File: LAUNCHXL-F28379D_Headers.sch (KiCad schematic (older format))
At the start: 7 parts, among them U1 AMP_DUE_SCH

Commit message: LTSpice Simulation Finished
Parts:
- C2, C5: symbol Device:C -> PCB_2020-rescue:C-Device
- H1, H2, H3, H4: symbol Mechanical:MountingHole -> PCB_2020-rescue:MountingHole-Mechanical
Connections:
- net labels added: +12V-power, +3V3-power, +5V-power, GND-power
- net labels removed: +12V, +3V3, +5V, GND
- wire segments 23 -> 21
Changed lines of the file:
@@
 $EndDescr
 $Comp
-L Mechanical:MountingHole H1
+L PCB_2020-rescue:MountingHole-Mechanical H1
 U 1 1 5E1FD379
 P 1150 2200
@@
 $EndComp
 $Comp
-L Mechanical:MountingHole H2
+L PCB_2020-rescue:MountingHole-Mechanical H2
 U 1 1 5E27C5D4
 P 1150 2500
@@
 $EndComp
 $Comp
-L Mechanical:MountingHole H3
+L PCB_2020-rescue:MountingHole-Mechanical H3
 U 1 1 5E27C92D
 P 1150 2800
@@
 $EndComp
 $Comp
-L Mechanical:MountingHole H4
+L PCB_2020-rescue:MountingHole-Mechanical H4
 U 1 1 5E27CB44
 P 1150 3100
@@
 Decoupling Caps
 $Comp
-L power:+3V3 #+3V2
+L PCB_2020-rescue:+3V3-power #+3V2
 U 1 1 684850F5
 P 3300 5700
@@
 AR Path="/5DF27589/684850F5" Ref="#+3V02"  Part="1"
 F 0 "#+3V02" H 3300 5700 50  0001 C CNN
-F 1 "+3V3" H 3150 5850 59  0000 L BNN
+F 1 "+3V3-power" H 3150 5850 59  0000 L BNN
 F 2 "" H 3300 5700 50  0001 C CNN
 F 3 "" H 3300 5700 50  0001 C CNN
@@
 $EndComp
 $Comp
-L Device:C C2
+L PCB_2020-rescue:C-Device C2
 U 1 1 6A2D04C9
 P 3300 6100
@@
 $EndComp
 $Comp
-L power:GND #GND3
+L PCB_2020-rescue:GND-power #GND3
 U 1 1 E2B99DEF
 P 4050 6500
@@
 AR Path="/5DF27589/E2B99DEF" Ref="#GND03"  Part="1"
 F 0 "#GND03" H 4050 6500 50  0001 C CNN
-F 1 "GND" H 3950 6300 59  0000 L BNN
+F 1 "GND-power" H 3950 6300 59  0000 L BNN
 F 2 "" H 4050 6500 50  0001 C CNN
 F 3 "" H 4050 6500 50  0001 C CNN
@@
 	1    0    0    -1
 $EndComp
-Wire Wire Line
-	3300 6500 4050 6500
-$Comp
-L Device:C C5
+$Comp
+L PCB_2020-rescue:C-Device C5
 U 1 1 6C4A4E38
 P 4750 6100
@@
 	4750 6250 4750 6500
 $Comp
-L power:+12V #PWR0101
+L PCB_2020-rescue:+12V-power #PWR0101
 U 1 1 5E5B7DE1
 P 4750 5700
 F 0 "#PWR0101" H 4750 5550 50  0001 C CNN
-F 1 "+12V" H 4650 5900 50  0000 L CNN
+F 1 "+12V-power" H 4650 5900 50  0000 L CNN
 F 2 "" H 4750 5700 50  0001 C CNN
 F 3 "" H 4750 5700 50  0001 C CNN
@@
 	3300 6250 3300 6500
 Connection ~ 4050 6500
-Wire Wire Line
-	4050 6500 4100 6500
-Wire Wire Line
-	4050 6500 4750 6500
 $Comp
 L PCB_2020:AMP_DUE_SCH U1
@@
 	8650 3400 8750 3400
 Wire Wire Line
-	7700 2750 7800 2750
-Connection ~ 7700 2750
-Wire Wire Line
 	7800 2750 7800 2850
-Wire Wire Line
-	7650 2750 7700 2750
 Wire Wire Line
 	7650 2850 7650 2750
@@
 KS1_CTL
 $Comp
-L power:+12V #PWR01
+L PCB_2020-rescue:+12V-power #PWR01
 U 1 1 5E686230
 P 7950 2850
 F 0 "#PWR01" H 7950 2700 50  0001 C CNN
-F 1 "+12V" H 7850 3050 50  0000 L CNN
+F 1 "+12V-power" H 7850 3050 50  0000 L CNN
 F 2 "" H 7950 2850 50  0001 C CNN
 F 3 "" H 7950 2850 50  0001 C CNN
@@
 $EndComp
 $Comp
-L power:+5V #P+?
+L PCB_2020-rescue:+5V-power #P+?
 U 1 1 5E684B6F
 P 7500 2850
@@
 AR Path="/5DF27589/5E684B6F" Ref="#P+06"  Part="1"
 F 0 "#P+06" H 7500 2850 50  0001 C CNN
-F 1 "+5V" H 7400 3000 59  0000 L BNN
+F 1 "+5V-power" H 7400 3000 59  0000 L BNN
 F 2 "" H 7500 2850 50  0001 C CNN
 F 3 "" H 7500 2850 50  0001 C CNN
@@
 $EndComp
 $Comp
-L power:GND #GND?
+L PCB_2020-rescue:GND-power #GND?
 U 1 1 5E681F81
 P 7700 2750
@@
 AR Path="/5DF27589/5E681F81" Ref="#GND04"  Part="1"
 F 0 "#GND04" H 7700 2750 50  0001 C CNN
-F 1 "GND" H 7600 2550 59  0000 L BNN
+F 1 "GND-power" H 7600 2550 59  0000 L BNN
 F 2 "" H 7700 2750 50  0001 C CNN
 F 3 "" H 7700 2750 50  0001 C CNN
@@
 Text GLabel 8750 3500 2    39   BiDi ~ 0
 SCIB_RX
+Wire Wire Line
+	3300 6500 4050 6500
+Wire Wire Line
+	7650 2750 7800 2750
+Wire Wire Line
+	4050 6500 4750 6500
 $EndSCHEMATC

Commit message: Updating PCB
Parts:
- removed U1: AMP_DUE_SCH, Drivetrain_control:Arduino DUE, symbol PCB_2020:AMP_DUE_SCH
- added U1: AMP_DUE_SCH, Drivetrain_control:Arduino DUE, symbol PCB_2020:AMP_DUE_SCH
- C2, C5: footprint Capacitor_SMD:C_0805_2012Metric_Pad1.15x1.40mm_HandSolder -> Capacitor_SMD:C_0805_2012Metric_Pad1.18x1.45mm_HandSolder
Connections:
- net +12V: now also U1.7 (GND)
- net +5V: now also U1.4 (3V3)
- net Brake_PWM_1: now also U1.78 (D9)
- net Brake_PWM_2: now also U1.77 (D8)
- net EN+_CTL: now also U1.47 (D29)
- net FS1_CTL: now also U1.53 (D41)
- net FWD_CTL: now also U1.56 (D47)
- net GND: now also U1.5 (5V), U1.6 (GND)
- net INPUT_A+_CTL: now also U1.50 (D35)
- net KS1_CTL: now also U1.59 (D53)
- net REV_CTL: now also U1.44 (D23)
- net SCIB_RX: now also U1.69 (RX0_0)
- net SCIB_TX: now also U1.70 (TX0_1)
- net STEERING: now also U1.76 (D7)
- net THROTTLE: now also U1.20 (A11)
- no-connect marks 2 -> 69
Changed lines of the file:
@@
 F 0 "C2" H 3360 6115 59  0000 L BNN
 F 1 "0.1uF" H 3360 5915 59  0000 L BNN
-F 2 "Capacitor_SMD:C_0805_2012Metric_Pad1.15x1.40mm_HandSolder" H 3300 6100 50  0001 C CNN
+F 2 "Capacitor_SMD:C_0805_2012Metric_Pad1.18x1.45mm_HandSolder" H 3300 6100 50  0001 C CNN
 F 3 "https://www.digikey.com/product-detail/en/samsung-electro-mechanics/CL21B104JBCNNNC/1276-1090-1-ND/3889176?utm_adgroup=Capacitors&slid=&pdv=c&pcrid=398891859082&productid=&utm_campaign=Dynamic+Search&mkwid=sK4nOncLn&utm_medium=cpc&utm_term=&gclid=CjwKCAiAmNbwBRBOEiwAqcwwpZSQgtNujl6BHsUYP-FQ70zdNcKZbQcVdbZiRuST7tQ2_ezynANN3xoCFdYQAvD_BwE&pmt=b&pkw=&utm_source=google" H 3300 6100 50  0001 C CNN
 	1    3300 6100
@@
 F 0 "C5" H 4810 6115 59  0000 L BNN
 F 1 "0.1uF" H 4810 5915 59  0000 L BNN
-F 2 "Capacitor_SMD:C_0805_2012Metric_Pad1.15x1.40mm_HandSolder" H 4750 6100 50  0001 C CNN
+F 2 "Capacitor_SMD:C_0805_2012Metric_Pad1.18x1.45mm_HandSolder" H 4750 6100 50  0001 C CNN
 F 3 "https://www.digikey.com/product-detail/en/samsung-electro-mechanics/CL21B104JBCNNNC/1276-1090-1-ND/3889176?utm_adgroup=Capacitors&slid=&pdv=c&pcrid=398891859082&productid=&utm_campaign=Dynamic+Search&mkwid=sK4nOncLn&utm_medium=cpc&utm_term=&gclid=CjwKCAiAmNbwBRBOEiwAqcwwpZSQgtNujl6BHsUYP-FQ70zdNcKZbQcVdbZiRuST7tQ2_ezynANN3xoCFdYQAvD_BwE&pmt=b&pkw=&utm_source=google" H 4750 6100 50  0001 C CNN
 	1    4750 6100
@@
 	3300 6250 3300 6500
 Connection ~ 4050 6500
-$Comp
-L PCB_2020:AMP_DUE_SCH U1
-U 6 1 5E7098FE
-P 7650 3400
-F 0 "U1" H 6606 3446 50  0000 R CNN
-F 1 "AMP_DUE_SCH" H 6606 3355 50  0000 R CNN
-F 2 "Drivetrain_control:Arduino DUE" H 7650 3400 50  0001 C CNN
-F 3 "" H 8200 3300 50  0001 C CNN
-	6    7650 3400
-	1    0    0    -1
-$EndComp
-NoConn ~ 7350 2850
-Wire Wire Line
-	8650 3500 8750 3500
-Wire Wire Line
-	8650 3400 8750 3400
-Wire Wire Line
-	7800 2750 7800 2850
-Wire Wire Line
-	7650 2850 7650 2750
-NoConn ~ 6650 3400
-Text GLabel 6950 4100 3    39   BiDi ~ 0
+Wire Wire Line
+	10500 3300 10600 3300
+Wire Wire Line
+	10500 3200 10600 3200
+Text GLabel 7000 4600 3    39   BiDi ~ 0
 KS1_CTL
 $Comp
 L PCB_2020-rescue:+12V-power #PWR01
 U 1 1 5E686230
-P 7950 2850
-F 0 "#PWR01" H 7950 2700 50  0001 C CNN
-F 1 "+12V-power" H 7850 3050 50  0000 L CNN
-F 2 "" H 7950 2850 50  0001 C CNN
-F 3 "" H 7950 2850 50  0001 C CNN
-	1    7950 2850
-	1    0    0    -1
+P 6050 2200
+F 0 "#PWR01" H 6050 2050 50  0001 C CNN
+F 1 "+12V-power" H 5950 2400 50  0000 L CNN
+F 2 "" H 6050 2200 50  0001 C CNN
+F 3 "" H 6050 2200 50  0001 C CNN
+	1    6050 2200
+	0    -1   -1   0
 $EndComp
 $Comp
 L PCB_2020-rescue:+5V-power #P+?
 U 1 1 5E684B6F
-P 7500 2850
+P 6350 1900
 AR Path="/5E684B6F" Ref="#P+?"  Part="1"
 AR Path="/5DF27589/5E684B6F" Ref="#P+06"  Part="1"
-F 0 "#P+06" H 7500 2850 50  0001 C CNN
-F 1 "+5V-power" H 7400 3000 59  0000 L BNN
-F 2 "" H 7500 2850 50  0001 C CNN
-F 3 "" H 7500 2850 50  0001 C CNN
-	1    7500 2850
-	1    0    0    -1
+F 0 "#P+06" H 6350 1900 50  0001 C CNN
+F 1 "+5V-power" H 6250 2050 59  0000 L BNN
+F 2 "" H 6350 1900 50  0001 C CNN
+F 3 "" H 6350 1900 50  0001 C CNN
+	1    6350 1900
+	0    -1   -1   0
 $EndComp
 $Comp
 L PCB_2020-rescue:GND-power #GND?
 U 1 1 5E681F81
-P 7700 2750
+P 6350 2100
 AR Path="/5E681F81" Ref="#GND?"  Part="1"
 AR Path="/5DF27589/5E681F81" Ref="#GND04"  Part="1"
-F 0 "#GND04" H 7700 2750 50  0001 C CNN
-F 1 "GND-power" H 7600 2550 59  0000 L BNN
-F 2 "" H 7700 2750 50  0001 C CNN
-F 3 "" H 7700 2750 50  0001 C CNN
-	1    7700 2750
-	-1   0    0    1
-$EndComp
-Wire Wire Line
-	8650 3300 8750 3300
-Wire Wire Line
-	8650 3200 8750 3200
-Wire Wire Line
-	8650 3100 8750 3100
-Wire Wire Line
-	6450 3300 6650 3300
-Text GLabel 6450 3300 0    39   Output ~ 0
+F 0 "#GND04" H 6350 2100 50  0001 C CNN
+F 1 "GND-power" H 6250 1900 59  0000 L BNN
+F 2 "" H 6350 2100 50  0001 C CNN
+F 3 "" H 6350 2100 50  0001 C CNN
+	1    6350 2100
+	0    1    1    0
+$EndComp
+Wire Wire Line
+	10500 2600 10600 2600
+Wire Wire Line
+	10500 2500 10600 2500
+Wire Wire Line
+	10500 2400 10600 2400
+Text GLabel 6450 3500 0    39   Output ~ 0
 THROTTLE
-Wire Wire Line
-	7250 3950 7250 4100
-Wire Wire Line
-	7550 3950 7550 4100
-Wire Wire Line
-	7850 3950 7850 4100
-Text GLabel 8450 4100 3    39   BiDi ~ 0
+Text GLabel 10000 4600 3    39   BiDi ~ 0
 REV_CTL
-Text GLabel 7250 4100 3    39   BiDi ~ 0
+Text GLabel 7600 4600 3    39   BiDi ~ 0
 FWD_CTL
-Text GLabel 7550 4100 3    39   BiDi ~ 0
+Text GLabel 8200 4600 3    39   BiDi ~ 0
 FS1_CTL
-Text GLabel 7850 4100 3    39   Input ~ 0
+Text GLabel 8800 4600 3    39   Input ~ 0
 INPUT_A+_CTL
-Text GLabel 8150 4100 3    39   Output ~ 0
+Text GLabel 9400 4600 3    39   Output ~ 0
 EN+_CTL
-Text GLabel 8750 3300 2    39   BiDi ~ 0
+Text GLabel 10600 2600 2    39   BiDi ~ 0
 STEERING
-Wire Wire Line
-	8450 4100 8450 3950
-Wire Wire Line
-	6950 4100 6950 3950
-Wire Wire Line
-	8150 4100 8150 3950
-Text GLabel 8750 3200 2    39   Output ~ 0
+Text GLabel 10600 2500 2    39   Output ~ 0
 Brake_PWM_2
-Text GLabel 8750 3100 2    39   Output ~ 0
+Text GLabel 10600 2400 2    39   Output ~ 0
 Brake_PWM_1
-Text GLabel 8750 3400 2    39   BiDi ~ 0
+Text GLabel 10600 3200 2    39   BiDi ~ 0
 SCIB_TX
-Text GLabel 8750 3500 2    39   BiDi ~ 0
+Text GLabel 10600 3300 2    39   BiDi ~ 0
 SCIB_RX
 Wire Wire Line
 	3300 6500 4050 6500
 Wire Wire Line
-	7650 2750 7800 2750
-Wire Wire Line
 	4050 6500 4750 6500
+$Comp
+L PCB_2020:AMP_DUE_SCH U1
+U 1 1 5F87F561
+P 8550 3050
+F 0 "U1" H 8550 4915 50  0000 C CNN
+F 1 "AMP_DUE_SCH" H 8550 4824 50  0000 C CNN
+F 2 "Drivetrain_control:Arduino DUE" H 8550 3050 50  0001 C CNN
+F 3 "" H 9100 2950 50  0001 C CNN
+	1    8550 3050
+	1    0    0    -1
+$EndComp
+Wire Wire Line
+	6450 3500 6600 3500
+Wire Wire Line
+	7000 4600 7000 4450
+Wire Wire Line
+	7600 4600 7600 4450
+Wire Wire Line
+	8200 4600 8200 4450
+Wire Wire Line
+	8800 4450 8800 4600
+Wire Wire Line
+	9400 4450 9400 4600
+Wire Wire Line
+	10000 4600 10000 4450
+Wire Wire Line
+	6350 1900 6600 1900
+Wire Wire Line
+	6350 2100 6500 2100
+Wire Wire Line
+	6500 2100 6500 2000
+Wire Wire Line
+	6500 2000 6600 2000
+Connection ~ 6500 2100
+Wire Wire Line
+	6500 2100 6600 2100
+Wire Wire Line
+	6050 2200 6600 2200
+NoConn ~ 6600 1600
+NoConn ~ 6600 1700
+NoConn ~ 6600 1800
+NoConn ~ 6600 2300
+NoConn ~ 6600 2400
+NoConn ~ 6600 2500
+NoConn ~ 6600 2600
+NoConn ~ 6600 2700
+NoConn ~ 6600 2800
+NoConn ~ 6600 2900
+NoConn ~ 6600 3000
+NoConn ~ 6600 3100
+NoConn ~ 6600 3200
+NoConn ~ 6600 3300
+NoConn ~ 6600 3400
+NoConn ~ 6600 3600
+NoConn ~ 6600 3700
+NoConn ~ 6600 3800
+NoConn ~ 6800 4450
+NoConn ~ 6900 4450
+NoConn ~ 7100 4450
+NoConn ~ 7200 4450
+NoConn ~ 7300 4450
+NoConn ~ 7400 4450
+NoConn ~ 7500 4450
+NoConn ~ 7700 4450
+NoConn ~ 7800 4450
+NoConn ~ 7900 4450
+NoConn ~ 8000 4450
+NoConn ~ 8100 4450
+NoConn ~ 8300 4450
+NoConn ~ 8400 4450
+NoConn ~ 8500 4450
+NoConn ~ 8600 4450
+NoConn ~ 8700 4450
+NoConn ~ 8900 4450
+NoConn ~ 9000 4450
+NoConn ~ 9100 4450
+NoConn ~ 9200 4450
+NoConn ~ 10500 1600
+NoConn ~ 10500 1700
+NoConn ~ 10500 1800
+NoConn ~ 10500 1900
+NoConn ~ 10500 2000
+NoConn ~ 10500 2100
+NoConn ~ 10500 2200
+NoConn ~ 10500 2300
+NoConn ~ 10500 2700
+NoConn ~ 10500 2800
+NoConn ~ 10500 2900
+NoConn ~ 10500 3000
+NoConn ~ 10500 3100
+NoConn ~ 10500 3400
+NoConn ~ 10500 3500
+NoConn ~ 10500 3600
+NoConn ~ 10500 3700
+NoConn ~ 10500 3800
+NoConn ~ 10500 3900
+NoConn ~ 10500 4000
+NoConn ~ 10500 4100
+NoConn ~ 9300 4450
+NoConn ~ 9500 4450
+NoConn ~ 9600 4450
+NoConn ~ 9700 4450
+NoConn ~ 9800 4450
+NoConn ~ 9900 4450
+NoConn ~ 10100 4450
+NoConn ~ 10200 4450
+NoConn ~ 10300 4450
 $EndSCHEMATC

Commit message: Working on PCB Routing for LoRa
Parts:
- added U4: LoRa, Drivetrain_control:LoRa, symbol PCB_2020-rescue:LoRa
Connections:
- net +3V3: now also U1.3 (IOREF), U4.48 (3V3)
- net GND: now also U4.49 (GND)
- no-connect marks 69 -> 68
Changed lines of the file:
@@
 NoConn ~ 6600 1600
 NoConn ~ 6600 1700
-NoConn ~ 6600 1800
 NoConn ~ 6600 2300
 NoConn ~ 6600 2400
@@
 NoConn ~ 10200 4450
 NoConn ~ 10300 4450
+$Comp
+L PCB_2020-rescue:LoRa U4
+U 1 1 5FA8EB82
+P 4050 3550
+F 0 "U4" H 4050 4615 50  0000 C CNN
+F 1 "LoRa" H 4050 4524 50  0000 C CNN
+F 2 "Drivetrain_control:LoRa" H 4050 3950 50  0001 C CNN
+F 3 "" H 4050 3950 50  0001 C CNN
+	1    4050 3550
+	1    0    0    -1
+$EndComp
+$Comp
+L PCB_2020-rescue:+3V3-power #PWR?
+U 1 1 5FAB7823
+P 6400 1800
+F 0 "#PWR?" H 6400 1650 50  0001 C CNN
+F 1 "+3V3-power" H 6415 1973 50  0000 C CNN
+F 2 "" H 6400 1800 50  0001 C CNN
+F 3 "" H 6400 1800 50  0001 C CNN
+	1    6400 1800
+	1    0    0    -1
+$EndComp
+Wire Wire Line
+	6400 1800 6600 1800
+Connection ~ 6300 2100
+$Comp
+L PCB_2020-rescue:GND-power #PWR?
+U 1 1 5FABAD06
+P 3500 3100
+F 0 "#PWR?" H 3500 2850 50  0001 C CNN
+F 1 "GND-power" V 3505 2973 50  0000 R CNN
+F 2 "" H 3500 3100 50  0001 C CNN
+F 3 "" H 3500 3100 50  0001 C CNN
+	1    3500 3100
+	0    1    1    0
+$EndComp
+$Comp
+L PCB_2020-rescue:+3V3-power #PWR?
+U 1 1 5FABBDB9
+P 3500 2900
+F 0 "#PWR?" H 3500 2750 50  0001 C CNN
+F 1 "+3V3-power" V 3515 3027 50  0000 L CNN
+F 2 "" H 3500 2900 50  0001 C CNN
+F 3 "" H 3500 2900 50  0001 C CNN
+	1    3500 2900
+	0    -1   -1   0
+$EndComp
 $EndSCHEMATC

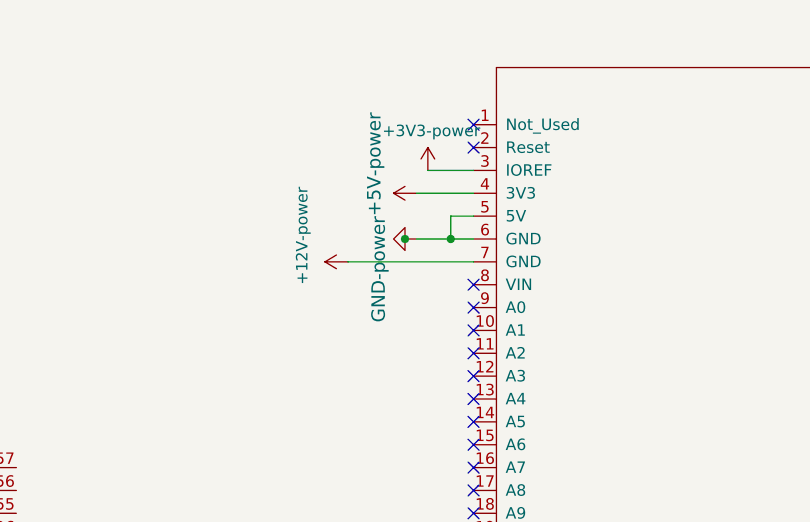
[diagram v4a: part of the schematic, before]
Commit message: Updating PCB with LoRa
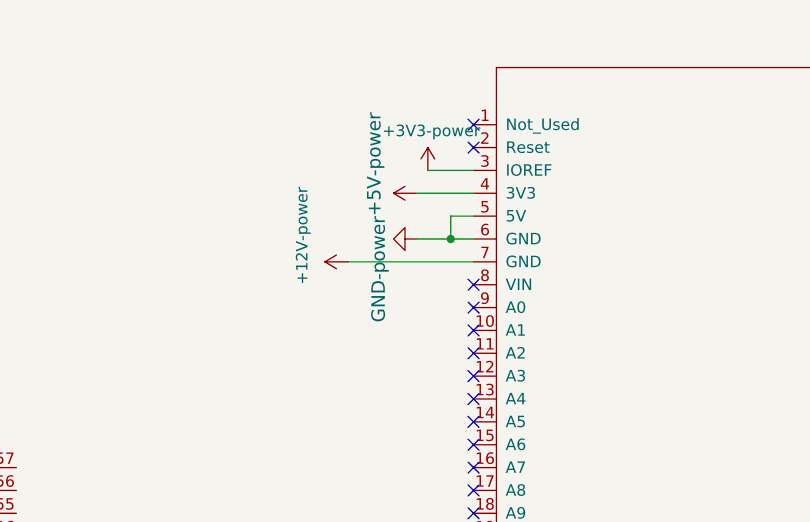
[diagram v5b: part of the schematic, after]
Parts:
- C2, C5: footprint Capacitor_SMD:C_0805_2012Metric_Pad1.18x1.45mm_HandSolder -> Capacitor_THT:C_Disc_D3.0mm_W1.6mm_P2.50mm
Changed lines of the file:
@@
 F 0 "C2" H 3360 6115 59  0000 L BNN
 F 1 "0.1uF" H 3360 5915 59  0000 L BNN
-F 2 "Capacitor_SMD:C_0805_2012Metric_Pad1.18x1.45mm_HandSolder" H 3300 6100 50  0001 C CNN
+F 2 "Capacitor_THT:C_Disc_D3.0mm_W1.6mm_P2.50mm" H 3300 6100 50  0001 C CNN
 F 3 "https://www.digikey.com/product-detail/en/samsung-electro-mechanics/CL21B104JBCNNNC/1276-1090-1-ND/3889176?utm_adgroup=Capacitors&slid=&pdv=c&pcrid=398891859082&productid=&utm_campaign=Dynamic+Search&mkwid=sK4nOncLn&utm_medium=cpc&utm_term=&gclid=CjwKCAiAmNbwBRBOEiwAqcwwpZSQgtNujl6BHsUYP-FQ70zdNcKZbQcVdbZiRuST7tQ2_ezynANN3xoCFdYQAvD_BwE&pmt=b&pkw=&utm_source=google" H 3300 6100 50  0001 C CNN
 	1    3300 6100
@@
 F 0 "C5" H 4810 6115 59  0000 L BNN
 F 1 "0.1uF" H 4810 5915 59  0000 L BNN
-F 2 "Capacitor_SMD:C_0805_2012Metric_Pad1.18x1.45mm_HandSolder" H 4750 6100 50  0001 C CNN
+F 2 "Capacitor_THT:C_Disc_D3.0mm_W1.6mm_P2.50mm" H 4750 6100 50  0001 C CNN
 F 3 "https://www.digikey.com/product-detail/en/samsung-electro-mechanics/CL21B104JBCNNNC/1276-1090-1-ND/3889176?utm_adgroup=Capacitors&slid=&pdv=c&pcrid=398891859082&productid=&utm_campaign=Dynamic+Search&mkwid=sK4nOncLn&utm_medium=cpc&utm_term=&gclid=CjwKCAiAmNbwBRBOEiwAqcwwpZSQgtNujl6BHsUYP-FQ70zdNcKZbQcVdbZiRuST7tQ2_ezynANN3xoCFdYQAvD_BwE&pmt=b&pkw=&utm_source=google" H 4750 6100 50  0001 C CNN
 	1    4750 6100
@@
 $EndComp
 $Comp
-L PCB_2020-rescue:+3V3-power #PWR?
+L PCB_2020-rescue:+3V3-power #PWR0108
 U 1 1 5FAB7823
 P 6400 1800
-F 0 "#PWR?" H 6400 1650 50  0001 C CNN
+F 0 "#PWR0108" H 6400 1650 50  0001 C CNN
 F 1 "+3V3-power" H 6415 1973 50  0000 C CNN
 F 2 "" H 6400 1800 50  0001 C CNN
@@
 Wire Wire Line
 	6400 1800 6600 1800
-Connection ~ 6300 2100
-$Comp
-L PCB_2020-rescue:GND-power #PWR?
+$Comp
+L PCB_2020-rescue:GND-power #PWR0109
 U 1 1 5FABAD06
 P 3500 3100
-F 0 "#PWR?" H 3500 2850 50  0001 C CNN
+F 0 "#PWR0109" H 3500 2850 50  0001 C CNN
 F 1 "GND-power" V 3505 2973 50  0000 R CNN
 F 2 "" H 3500 3100 50  0001 C CNN
@@
 $EndComp
 $Comp
-L PCB_2020-rescue:+3V3-power #PWR?
+L PCB_2020-rescue:+3V3-power #PWR0110
 U 1 1 5FABBDB9
 P 3500 2900
-F 0 "#PWR?" H 3500 2750 50  0001 C CNN
+F 0 "#PWR0110" H 3500 2750 50  0001 C CNN
 F 1 "+3V3-power" V 3515 3027 50  0000 L CNN
 F 2 "" H 3500 2900 50  0001 C CNN
